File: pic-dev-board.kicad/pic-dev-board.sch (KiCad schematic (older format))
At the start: 42 parts, among them J1 Conn_01x03_Male, J15 Barrel_Jack_Switch, J16 RUN/~PGM, J17 I2C, J18 GP1(RA1)/RB6, J19 GP2(RA2)/RB4, J2 Conn_01x03_Male, J3 Conn_01x03_Male, J4 Conn_01x03_Male, J5 Conn_01x03_Male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

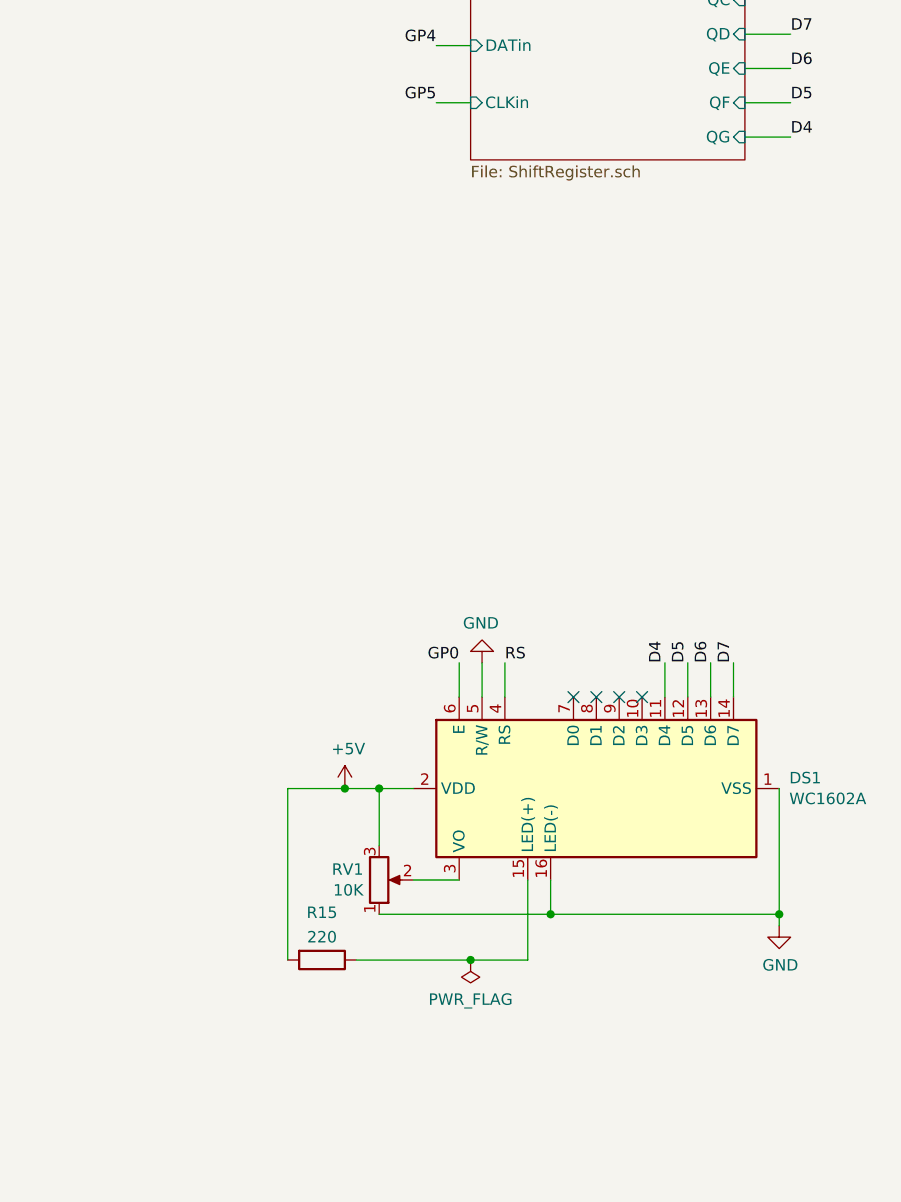
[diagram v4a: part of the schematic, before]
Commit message: added second shift-register
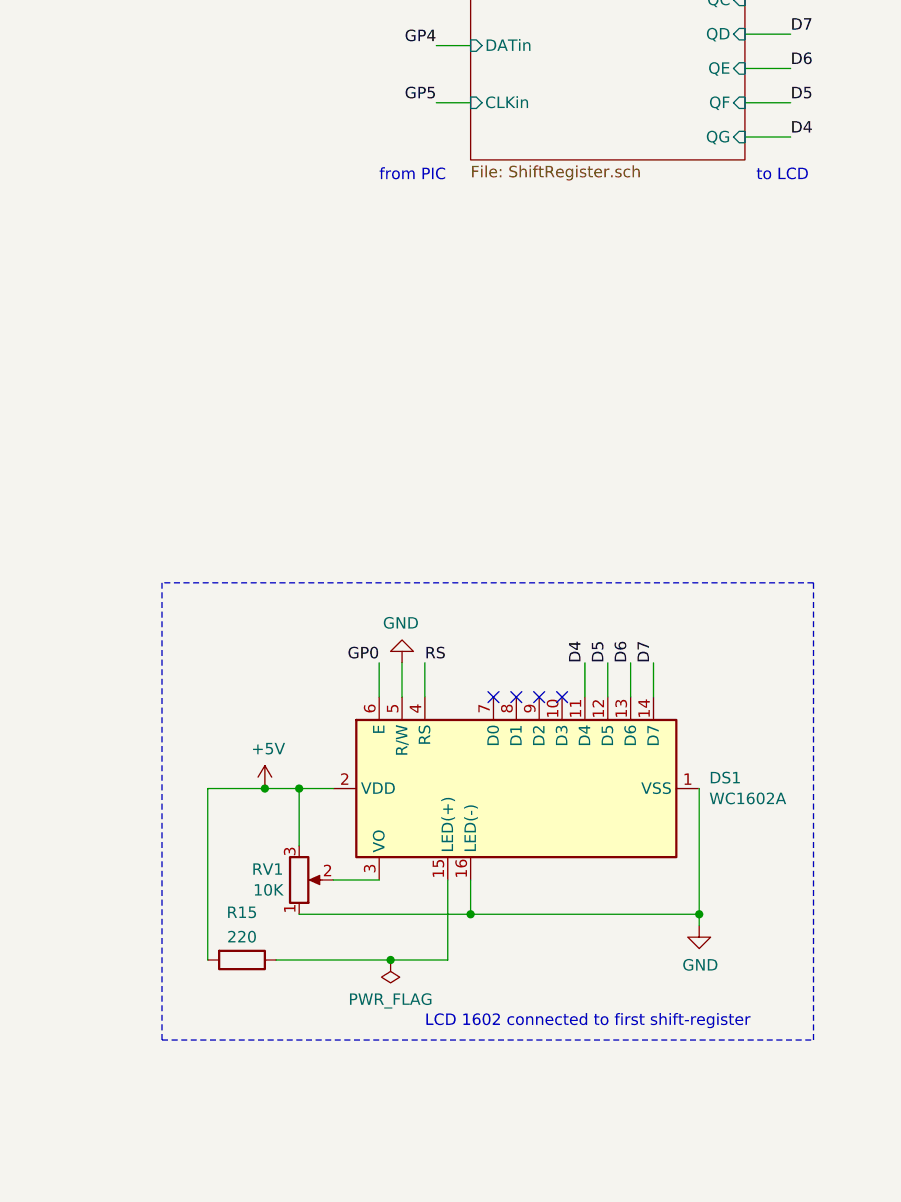
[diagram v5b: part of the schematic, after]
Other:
- note added: "LCD 1602 connected to first shift-register"
- note added: "from PIC"
- note added: "to LCD"
- moved on the sheet: DS1, R15, RV1
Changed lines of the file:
@@
 L power:GND #PWR015
 U 1 1 5F320655
-P 10700 5050
-F 0 "#PWR015" H 10700 4800 50  0001 C CNN
-F 1 "GND" H 10705 4877 50  0000 C CNN
-F 2 "" H 10700 5050 50  0001 C CNN
-F 3 "" H 10700 5050 50  0001 C CNN
-	1    10700 5050
+P 10350 5050
+F 0 "#PWR015" H 10350 4800 50  0001 C CNN
+F 1 "GND" H 10355 4877 50  0000 C CNN
+F 2 "" H 10350 5050 50  0001 C CNN
+F 3 "" H 10350 5050 50  0001 C CNN
+	1    10350 5050
 	1    0    0    -1
 $EndComp
@@
 L Display_Character:WC1602A DS1
 U 1 1 5F32065D
-P 9900 4450
-F 0 "DS1" V 9854 3606 50  0000 R CNN
-F 1 "WC1602A" V 9945 3606 50  0000 R CNN
-F 2 "Display:WC1602A" H 9900 3550 50  0001 C CIN
-F 3 "http://www.wincomlcd.com/pdf/WC1602A-SFYLYHTC06.pdf" H 10600 4450 50  0001 C CNN
-	1    9900 4450
+P 9550 4450
+F 0 "DS1" V 9504 3606 50  0000 R CNN
+F 1 "WC1602A" V 9595 3606 50  0000 R CNN
+F 2 "Display:WC1602A" H 9550 3550 50  0001 C CIN
+F 3 "http://www.wincomlcd.com/pdf/WC1602A-SFYLYHTC06.pdf" H 10250 4450 50  0001 C CNN
+	1    9550 4450
 	0    -1   1    0
 $EndComp
 Wire Wire Line
-	10700 4450 10700 5000
-Connection ~ 10700 5000
-Wire Wire Line
-	10700 5000 10700 5050
+	10350 4450 10350 5000
+Connection ~ 10350 5000
+Wire Wire Line
+	10350 5000 10350 5050
 $Comp
 L Device:R R15
 U 1 1 5F320671
-P 8700 5200
-F 0 "R15" V 8493 5200 50  0000 C CNN
-F 1 "220" V 8600 5200 50  0000 C CNN
-F 2 "" V 8630 5200 50  0001 C CNN
-F 3 "~" H 8700 5200 50  0001 C CNN
-	1    8700 5200
+P 8350 5200
+F 0 "R15" V 8143 5200 50  0000 C CNN
+F 1 "220" V 8250 5200 50  0000 C CNN
+F 2 "" V 8280 5200 50  0001 C CNN
+F 3 "~" H 8350 5200 50  0001 C CNN
+	1    8350 5200
 	0    1    1    0
 $EndComp
 Wire Wire Line
-	9700 4850 9700 5000
-Connection ~ 9700 5000
-Wire Wire Line
-	9700 5000 10700 5000
-Wire Wire Line
-	9600 4850 9600 5200
-Wire Wire Line
-	8550 4450 8800 4450
-Wire Wire Line
-	9600 5200 9350 5200
+	9350 4850 9350 5000
+Connection ~ 9350 5000
+Wire Wire Line
+	9350 5000 10350 5000
+Wire Wire Line
+	9250 4850 9250 5200
+Wire Wire Line
+	8200 4450 8450 4450
+Wire Wire Line
+	9250 5200 9000 5200
 $Comp
 L Device:R_POT RV1
 U 1 1 5F320680
-P 8950 4850
-F 0 "RV1" H 8881 4804 50  0000 R CNN
-F 1 "10K" H 8881 4895 50  0000 R CNN
-F 2 "" H 8950 4850 50  0001 C CNN
-F 3 "~" H 8950 4850 50  0001 C CNN
-	1    8950 4850
+P 8600 4850
+F 0 "RV1" H 8531 4804 50  0000 R CNN
+F 1 "10K" H 8531 4895 50  0000 R CNN
+F 2 "" H 8600 4850 50  0001 C CNN
+F 3 "~" H 8600 4850 50  0001 C CNN
+	1    8600 4850
 	1    0    0    1
 $EndComp
 Wire Wire Line
-	8950 5000 9700 5000
-Wire Wire Line
-	9300 4850 9100 4850
-Wire Wire Line
-	8950 4700 8950 4450
-Connection ~ 8950 4450
-Wire Wire Line
-	8950 4450 9100 4450
+	8600 5000 9350 5000
+Wire Wire Line
+	8950 4850 8750 4850
+Wire Wire Line
+	8600 4700 8600 4450
+Connection ~ 8600 4450
+Wire Wire Line
+	8600 4450 8750 4450
 $Comp
 L Connector:Conn_01x06_Male J6
@@
 Text Label 6700 5050 0    50   ~ 0
 RC7
-Text Label 9300 3900 2    50   ~ 0
+Text Label 8950 3900 2    50   ~ 0
 GP0
 Wire Wire Line
-	9300 3900 9300 4050
-NoConn ~ 9800 4050
-NoConn ~ 9900 4050
-NoConn ~ 10000 4050
-NoConn ~ 10100 4050
+	8950 3900 8950 4050
+NoConn ~ 9450 4050
+NoConn ~ 9550 4050
+NoConn ~ 9650 4050
+NoConn ~ 9750 4050
 $Comp
 L power:GND #PWR0101
 U 1 1 5F3AB743
-P 9400 3900
-F 0 "#PWR0101" H 9400 3650 50  0001 C CNN
-F 1 "GND" H 9405 3727 50  0000 C CNN
-F 2 "" H 9400 3900 50  0001 C CNN
-F 3 "" H 9400 3900 50  0001 C CNN
-	1    9400 3900
-	-1   0    0    1
-$EndComp
-Wire Wire Line
-	9400 4050 9400 3900
+P 9050 3900
+F 0 "#PWR0101" H 9050 3650 50  0001 C CNN
+F 1 "GND" H 9055 3727 50  0000 C CNN
+F 2 "" H 9050 3900 50  0001 C CNN
+F 3 "" H 9050 3900 50  0001 C CNN
+	1    9050 3900
+	-1   0    0    1
+$EndComp
+Wire Wire Line
+	9050 4050 9050 3900
 Text Label 9200 1200 2    50   ~ 0
 GP4
@@
 Wire Wire Line
 	9200 1450 9350 1450
-Text Label 9500 3900 0    50   ~ 0
+Text Label 9150 3900 0    50   ~ 0
 RS
 Wire Wire Line
-	9500 4050 9500 3900
+	9150 4050 9150 3900
 Text Label 10750 1000 0    50   ~ 0
 RS
 Wire Wire Line
 	10550 1000 10750 1000
-Text Label 10500 3900 1    50   ~ 0
+Text Label 10150 3900 1    50   ~ 0
 D7
 Text Label 10750 1150 0    50   ~ 0
 D7
-Text Label 10400 3900 1    50   ~ 0
+Text Label 10050 3900 1    50   ~ 0
 D6
 Text Label 10750 1300 0    50   ~ 0
 D6
-Text Label 10300 3900 1    50   ~ 0
+Text Label 9950 3900 1    50   ~ 0
 D5
-Text Label 10200 3900 1    50   ~ 0
+Text Label 9850 3900 1    50   ~ 0
 D4
 Text Label 10750 1450 0    50   ~ 0
@@
 	10750 1150 10550 1150
 Wire Wire Line
-	10500 3900 10500 4050
-Wire Wire Line
-	10400 3900 10400 4050
-Wire Wire Line
-	10300 3900 10300 4050
-Wire Wire Line
-	10200 3900 10200 4050
+	10150 3900 10150 4050
+Wire Wire Line
+	10050 3900 10050 4050
+Wire Wire Line
+	9950 3900 9950 4050
+Wire Wire Line
+	9850 3900 9850 4050
 $Comp
 L power:+5V #PWR0102
 U 1 1 5F3D7A4C
-P 8800 4450
-F 0 "#PWR0102" H 8800 4300 50  0001 C CNN
-F 1 "+5V" H 8815 4623 50  0000 C CNN
-F 2 "" H 8800 4450 50  0001 C CNN
-F 3 "" H 8800 4450 50  0001 C CNN
-	1    8800 4450
-	1    0    0    -1
-$EndComp
-Connection ~ 8800 4450
-Wire Wire Line
-	8800 4450 8950 4450
+P 8450 4450
+F 0 "#PWR0102" H 8450 4300 50  0001 C CNN
+F 1 "+5V" H 8465 4623 50  0000 C CNN
+F 2 "" H 8450 4450 50  0001 C CNN
+F 3 "" H 8450 4450 50  0001 C CNN
+	1    8450 4450
+	1    0    0    -1
+$EndComp
+Connection ~ 8450 4450
+Wire Wire Line
+	8450 4450 8600 4450
 Wire Wire Line
 	5350 4050 5200 4050
@@
 $EndComp
 Wire Wire Line
-	8550 4450 8550 5200
+	8200 4450 8200 5200
 $Comp
 L power:PWR_FLAG #FLG0103
 U 1 1 5F3F9EE7
-P 9350 5200
-F 0 "#FLG0103" H 9350 5275 50  0001 C CNN
-F 1 "PWR_FLAG" H 9350 5373 50  0000 C CNN
-F 2 "" H 9350 5200 50  0001 C CNN
-F 3 "~" H 9350 5200 50  0001 C CNN
-	1    9350 5200
-	-1   0    0    1
-$EndComp
-Connection ~ 9350 5200
-Wire Wire Line
-	9350 5200 8850 5200
+P 9000 5200
+F 0 "#FLG0103" H 9000 5275 50  0001 C CNN
+F 1 "PWR_FLAG" H 9000 5373 50  0000 C CNN
+F 2 "" H 9000 5200 50  0001 C CNN
+F 3 "~" H 9000 5200 50  0001 C CNN
+	1    9000 5200
+	-1   0    0    1
+$EndComp
+Connection ~ 9000 5200
+Wire Wire Line
+	9000 5200 8500 5200
 $Comp
 L Connector:Barrel_Jack_Switch J15
@@
 Text Notes 1950 7350 0    50   ~ 0
 External connectors
+Text Notes 9150 5500 0    50   ~ 0
+LCD 1602 connected to first shift-register
+Wire Notes Line
+	10850 5550 10850 3550
+Wire Notes Line
+	10850 3550 8000 3550
+Wire Notes Line
+	8000 3550 8000 5550
+Wire Notes Line
+	8000 5550 10850 5550
+Text Notes 8950 1800 0    50   ~ 0
+from PIC
+Text Notes 10600 1800 0    50   ~ 0
+to LCD
 $EndSCHEMATC

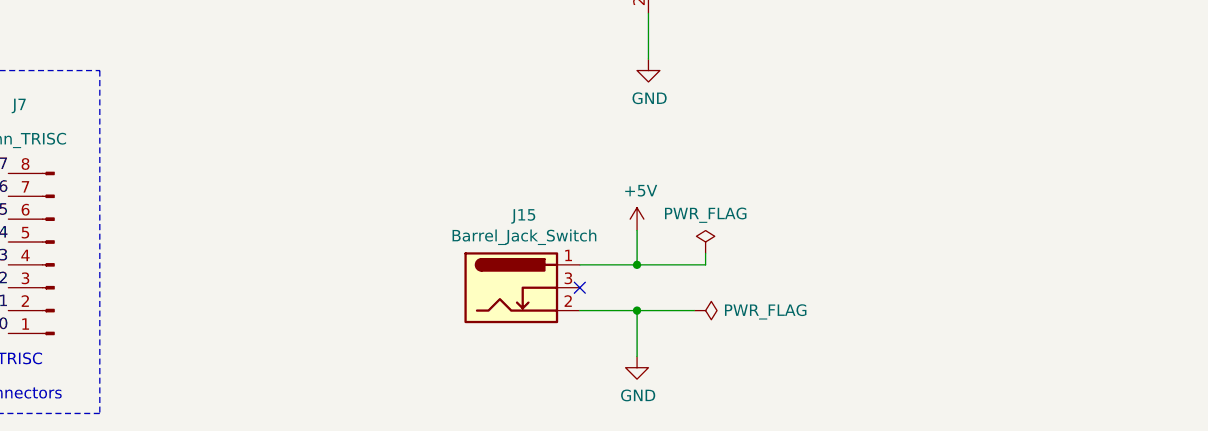
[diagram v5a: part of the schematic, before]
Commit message: added +5V/GND connectors
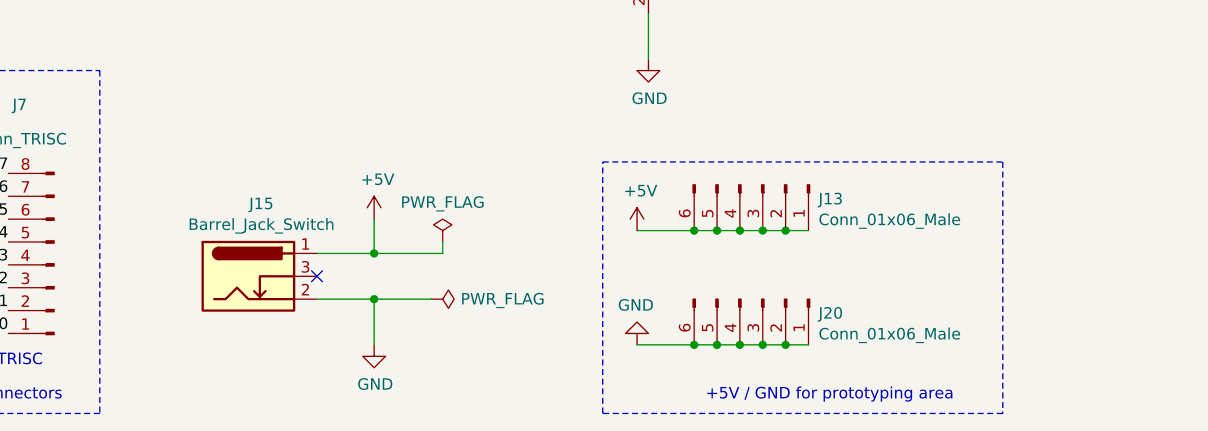
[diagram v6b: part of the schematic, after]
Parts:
- added J13, J20: Conn_01x06_Male, symbol Connector:Conn_01x06_Male
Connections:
- net +5V: now also J13.1 (Pin_1), J13.2 (Pin_2), J13.3 (Pin_3), J13.4 (Pin_4), J13.5 (Pin_5), J13.6 (Pin_6)
- net GND: now also J20.1 (Pin_1), J20.2 (Pin_2), J20.3 (Pin_3), J20.4 (Pin_4), J20.5 (Pin_5), J20.6 (Pin_6)
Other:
- note added: "+5V / GND for prototyping area"
- moved on the sheet: J15
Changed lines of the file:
@@
 L power:PWR_FLAG #FLG0101
 U 1 1 5F3F0293
-P 5400 6950
-F 0 "#FLG0101" H 5400 7025 50  0001 C CNN
-F 1 "PWR_FLAG" V 5400 7078 50  0000 L CNN
-F 2 "" H 5400 6950 50  0001 C CNN
-F 3 "~" H 5400 6950 50  0001 C CNN
-	1    5400 6950
+P 4250 6900
+F 0 "#FLG0101" H 4250 6975 50  0001 C CNN
+F 1 "PWR_FLAG" V 4250 7028 50  0000 L CNN
+F 2 "" H 4250 6900 50  0001 C CNN
+F 3 "~" H 4250 6900 50  0001 C CNN
+	1    4250 6900
 	0    1    1    0
 $EndComp
@@
 L power:PWR_FLAG #FLG0102
 U 1 1 5F3F0E86
-P 5450 6700
-F 0 "#FLG0102" H 5450 6775 50  0001 C CNN
-F 1 "PWR_FLAG" H 5450 6873 50  0000 C CNN
-F 2 "" H 5450 6700 50  0001 C CNN
-F 3 "~" H 5450 6700 50  0001 C CNN
-	1    5450 6700
+P 4300 6650
+F 0 "#FLG0102" H 4300 6725 50  0001 C CNN
+F 1 "PWR_FLAG" H 4300 6823 50  0000 C CNN
+F 2 "" H 4300 6650 50  0001 C CNN
+F 3 "~" H 4300 6650 50  0001 C CNN
+	1    4300 6650
 	1    0    0    -1
 $EndComp
@@
 L Connector:Barrel_Jack_Switch J15
 U 1 1 5F353FBE
-P 4600 6850
-F 0 "J15" H 4657 7167 50  0000 C CNN
-F 1 "Barrel_Jack_Switch" H 4657 7076 50  0000 C CNN
-F 2 "" H 4650 6810 50  0001 C CNN
-F 3 "~" H 4650 6810 50  0001 C CNN
-	1    4600 6850
-	1    0    0    -1
-$EndComp
-NoConn ~ 4900 6850
+P 3450 6800
+F 0 "J15" H 3507 7117 50  0000 C CNN
+F 1 "Barrel_Jack_Switch" H 3507 7026 50  0000 C CNN
+F 2 "" H 3500 6760 50  0001 C CNN
+F 3 "~" H 3500 6760 50  0001 C CNN
+	1    3450 6800
+	1    0    0    -1
+$EndComp
+NoConn ~ 3750 6800
 $Comp
 L power:GND #PWR0103
 U 1 1 5F362EB6
-P 5150 7150
-F 0 "#PWR0103" H 5150 6900 50  0001 C CNN
-F 1 "GND" H 5155 6977 50  0000 C CNN
-F 2 "" H 5150 7150 50  0001 C CNN
-F 3 "" H 5150 7150 50  0001 C CNN
-	1    5150 7150
+P 4000 7100
+F 0 "#PWR0103" H 4000 6850 50  0001 C CNN
+F 1 "GND" H 4005 6927 50  0000 C CNN
+F 2 "" H 4000 7100 50  0001 C CNN
+F 3 "" H 4000 7100 50  0001 C CNN
+	1    4000 7100
 	1    0    0    -1
 $EndComp
@@
 L power:+5V #PWR0104
 U 1 1 5F363A77
-P 5150 6600
-F 0 "#PWR0104" H 5150 6450 50  0001 C CNN
-F 1 "+5V" H 5165 6773 50  0000 C CNN
-F 2 "" H 5150 6600 50  0001 C CNN
-F 3 "" H 5150 6600 50  0001 C CNN
-	1    5150 6600
-	1    0    0    -1
-$EndComp
-Wire Wire Line
-	4900 6750 5150 6750
-Wire Wire Line
-	5150 6750 5150 6600
-Wire Wire Line
-	4900 6950 5150 6950
-Wire Wire Line
-	5150 6950 5150 7150
-Wire Wire Line
-	5150 6750 5450 6750
-Wire Wire Line
-	5450 6750 5450 6700
-Connection ~ 5150 6750
+P 4000 6550
+F 0 "#PWR0104" H 4000 6400 50  0001 C CNN
+F 1 "+5V" H 4015 6723 50  0000 C CNN
+F 2 "" H 4000 6550 50  0001 C CNN
+F 3 "" H 4000 6550 50  0001 C CNN
+	1    4000 6550
+	1    0    0    -1
+$EndComp
+Wire Wire Line
+	3750 6700 4000 6700
+Wire Wire Line
+	4000 6700 4000 6550
+Wire Wire Line
+	3750 6900 4000 6900
+Wire Wire Line
+	4000 6900 4000 7100
+Wire Wire Line
+	4000 6700 4300 6700
+Wire Wire Line
+	4300 6700 4300 6650
+Connection ~ 4000 6700
 Wire Wire Line
 	5200 5650 5200 5850
 Wire Wire Line
-	5150 6950 5400 6950
-Connection ~ 5150 6950
+	4000 6900 4250 6900
+Connection ~ 4000 6900
 $Comp
 L Connector:Conn_01x02_Male J16
@@
 Text Notes 10600 1800 0    50   ~ 0
 to LCD
+$Comp
+L Connector:Conn_01x06_Male J13
+U 1 1 5F40173F
+P 5700 6400
+F 0 "J13" V 5762 6644 50  0000 L CNN
+F 1 "Conn_01x06_Male" V 5853 6644 50  0000 L CNN
+F 2 "" H 5700 6400 50  0001 C CNN
+F 3 "~" H 5700 6400 50  0001 C CNN
+	1    5700 6400
+	0    1    1    0
+$EndComp
+$Comp
+L Connector:Conn_01x06_Male J20
+U 1 1 5F402982
+P 5700 6900
+F 0 "J20" V 5762 7144 50  0000 L CNN
+F 1 "Conn_01x06_Male" V 5853 7144 50  0000 L CNN
+F 2 "" H 5700 6900 50  0001 C CNN
+F 3 "~" H 5700 6900 50  0001 C CNN
+	1    5700 6900
+	0    1    1    0
+$EndComp
+$Comp
+L power:+5V #PWR028
+U 1 1 5F403557
+P 5150 6600
+F 0 "#PWR028" H 5150 6450 50  0001 C CNN
+F 1 "+5V" H 5165 6773 50  0000 C CNN
+F 2 "" H 5150 6600 50  0001 C CNN
+F 3 "" H 5150 6600 50  0001 C CNN
+	1    5150 6600
+	1    0    0    -1
+$EndComp
+$Comp
+L power:GND #PWR029
+U 1 1 5F403BD0
+P 5150 7100
+F 0 "#PWR029" H 5150 6850 50  0001 C CNN
+F 1 "GND" H 5155 6927 50  0000 C CNN
+F 2 "" H 5150 7100 50  0001 C CNN
+F 3 "" H 5150 7100 50  0001 C CNN
+	1    5150 7100
+	-1   0    0    1
+$EndComp
+Wire Wire Line
+	5150 6600 5400 6600
+Connection ~ 5400 6600
+Wire Wire Line
+	5400 6600 5500 6600
+Connection ~ 5500 6600
+Wire Wire Line
+	5500 6600 5600 6600
+Connection ~ 5600 6600
+Wire Wire Line
+	5600 6600 5700 6600
+Connection ~ 5700 6600
+Wire Wire Line
+	5700 6600 5800 6600
+Connection ~ 5800 6600
+Wire Wire Line
+	5800 6600 5900 6600
+Wire Wire Line
+	5150 7100 5400 7100
+Connection ~ 5400 7100
+Wire Wire Line
+	5400 7100 5500 7100
+Connection ~ 5500 7100
+Wire Wire Line
+	5500 7100 5600 7100
+Connection ~ 5600 7100
+Wire Wire Line
+	5600 7100 5700 7100
+Connection ~ 5700 7100
+Wire Wire Line
+	5700 7100 5800 7100
+Connection ~ 5800 7100
+Wire Wire Line
+	5800 7100 5900 7100
+Wire Notes Line
+	5000 6300 6750 6300
+Wire Notes Line
+	6750 6300 6750 7400
+Wire Notes Line
+	6750 7400 5000 7400
+Wire Notes Line
+	5000 7400 5000 6300
+Text Notes 5450 7350 0    50   ~ 0
++5V / GND for prototyping area
 $EndSCHEMATC
